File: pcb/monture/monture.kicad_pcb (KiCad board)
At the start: 2 copper layers, 150 x 110 mm, 72 parts, among them U1 Teensy 4.1

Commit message: PCB monture : deux cartes, StepStick et drivers externes
Carte StepStick (pcb/monture) :
- Selecteur retire (SW_SEL, RN_SEL, 74HC126/74HCT125, pastilles EXT) :
  les supports sont pilotes directement par le Teensy ; rappels RN_EN
  (10k vers 3,3V) pour garder les drivers coupes au demarrage.
- Ponts SPI TMC5160 conserves (decales de 0,1 mm : courtyards KiCad 10).
- Re-routage Freerouting, buck manuel conserve : DRC 0 erreur, 0 non
  connecte. Assemblage FreeCAD : modele PCB reimporte, 0 collision.

Carte drivers externes (pcb/monture_ext, nouvelle) :
- Par axe : bornier J_VM (VM, GND) et bornier J_SIG (EN, STEP, DIR, GND)
  en 5 V via 3 x 74HCT125 ; 220 uF par sortie VM ; plans GND et +36V.
- Meme format, fixations, connecteurs et brochage Teensy que la carte
  StepStick. DRC 0 erreur, 0 non connecte.
- Boitier 35 mm (boitier_monture_ext.scad), STL, rendus, assemblage
  FreeCAD controle.

build_kicad_pcbs.py genere les deux cartes (blocs communs) et reproduit
exactement les cartes routees. README et fiche technique mis a jour.

Co-Authored-By: Claude Opus 5.5 <noreply@anthropic.com>
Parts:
- removed C_EXT_DIR, C_EXT_EN, C_EXT_STEP, C_INT_DIR, C_INT_EN, C_INT_STEP: 100nF, C_Disc_D3.0mm_W1.6mm_P2.50mm
- removed EXT_ALT, EXT_AZ, EXT_DEROT, EXT_FOCUS: Ext. Driver, SolderWire-0.5sqmm_1x04_P4.6mm_D0.9mm_OD2.1mm
- removed RN_SEL: 10k x8 (commun broche 1), R_Array_SIP9
- removed SW_SEL: DIP x4, SW_DIP_SPSTx04_Slide_9.78x12.34mm_W7.62mm_P2.54mm
- removed U_EXT_DIR, U_EXT_EN, U_EXT_STEP: 74HCT125, DIP-14_W7.62mm
- removed U_INT_DIR, U_INT_EN, U_INT_STEP: 74HC126, DIP-14_W7.62mm
- added RN_EN: 10k x4 (commun broche 1), R_Array_SIP5, F.Cu at (108.0, 57.6)
- moved JP_DEROT_CLK 0.10 mm to (87.2, 48.7)
- moved JP_DEROT_CSN 0.10 mm to (87.2, 43.6)
- moved JP_DEROT_SCK 0.10 mm to (87.2, 41.1)
- moved JP_DEROT_SDI 0.10 mm to (87.2, 38.5)
- moved JP_DEROT_SDO 0.10 mm to (87.2, 46.2)
- moved JP_FOCUS_CLK 0.10 mm to (117.2, 48.7)
- moved JP_FOCUS_CSN 0.10 mm to (117.2, 43.6)
- moved JP_FOCUS_SCK 0.10 mm to (117.2, 41.1)
- moved JP_FOCUS_SDI 0.10 mm to (117.2, 38.5)
- moved JP_FOCUS_SDO 0.10 mm to (117.2, 46.2)
- moved JP_ALT_CLK 0.10 mm to (57.1, 48.7)
- moved JP_ALT_CSN 0.10 mm to (57.1, 43.6)
- moved JP_ALT_SCK 0.10 mm to (57.1, 41.1)
- moved JP_ALT_SDI 0.10 mm to (57.1, 38.5)
- moved JP_ALT_SDO 0.10 mm to (57.1, 46.2)
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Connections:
- DRV_ALT_L pad 1: ALT_EN_INT -> ALT_EN
- DRV_ALT_L pad 7: ALT_STEP_INT -> ALT_STEP
- DRV_ALT_L pad 8: ALT_DIR_INT -> ALT_DIR
- DRV_AZ_L pad 1: AZ_EN_INT -> AZ_EN
- DRV_AZ_L pad 7: AZ_STEP_INT -> AZ_STEP
- DRV_AZ_L pad 8: AZ_DIR_INT -> AZ_DIR
- DRV_DEROT_L pad 1: DEROT_EN_INT -> DEROT_EN
- DRV_DEROT_L pad 7: DEROT_STEP_INT -> DEROT_STEP
- DRV_DEROT_L pad 8: DEROT_DIR_INT -> DEROT_DIR
- DRV_FOCUS_L pad 1: FOCUS_EN_INT -> FOCUS_EN
- DRV_FOCUS_L pad 7: FOCUS_STEP_INT -> FOCUS_STEP
- DRV_FOCUS_L pad 8: FOCUS_DIR_INT -> FOCUS_DIR
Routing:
- net GND: track 733.1 -> 542.4 mm
- net AZ_EN_EXT: track 152.4 -> 0.00 mm, vias 1 -> 0
- net FOCUS_STEP_EXT: track 148.1 -> 0.00 mm, vias 2 -> 0
- net SEL_AZ: track 139.0 -> 0.00 mm
- net SEL_ALT: track 133.0 -> 0.00 mm, vias 2 -> 0
- net AZ_EN_INT: track 126.7 -> 0.00 mm
- net ALT_EN_EXT: track 124.2 -> 0.00 mm, vias 2 -> 0
- net SEL_FOCUS: track 123.1 -> 0.00 mm
- net SEL_DEROT: track 121.6 -> 0.00 mm
- net AZ_DIR_EXT: track 118.4 -> 0.00 mm, vias 2 -> 0
- net FOCUS_DIR_EXT: track 118.2 -> 0.00 mm, vias 1 -> 0
- net ALT_EN_INT: track 114.4 -> 0.00 mm, vias 3 -> 0
- net DEROT_STEP_EXT: track 104.1 -> 0.00 mm, vias 2 -> 0
- net FOCUS_EN_EXT: track 101.7 -> 0.00 mm, vias 1 -> 0
- net ALT_DIR_EXT: track 96.5 -> 0.00 mm, vias 3 -> 0
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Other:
- outline, holes or cut-outs redrawn
- board text added: "RAPPELS EN"
- board text removed: "ALT"
- board text removed: "AZ"
- board text removed: "DER"
- board text removed: "DIR"
- board text removed: "DRIVER EXT. 5V"
- board text removed: "FOC"
- board text removed: "GND"
- board text removed: "ON = EXTERNE 5V / OFF = STEPSTICK"
- board text removed: "SELECTEUR DRIVERS"
- board text removed: "STEP"
- board text removed: "TAMPONS DRIVERS EXTERNES 5V (74HCT125)"
- board text removed: "TAMPONS STEPSTICK 3,3V (74HC126)"

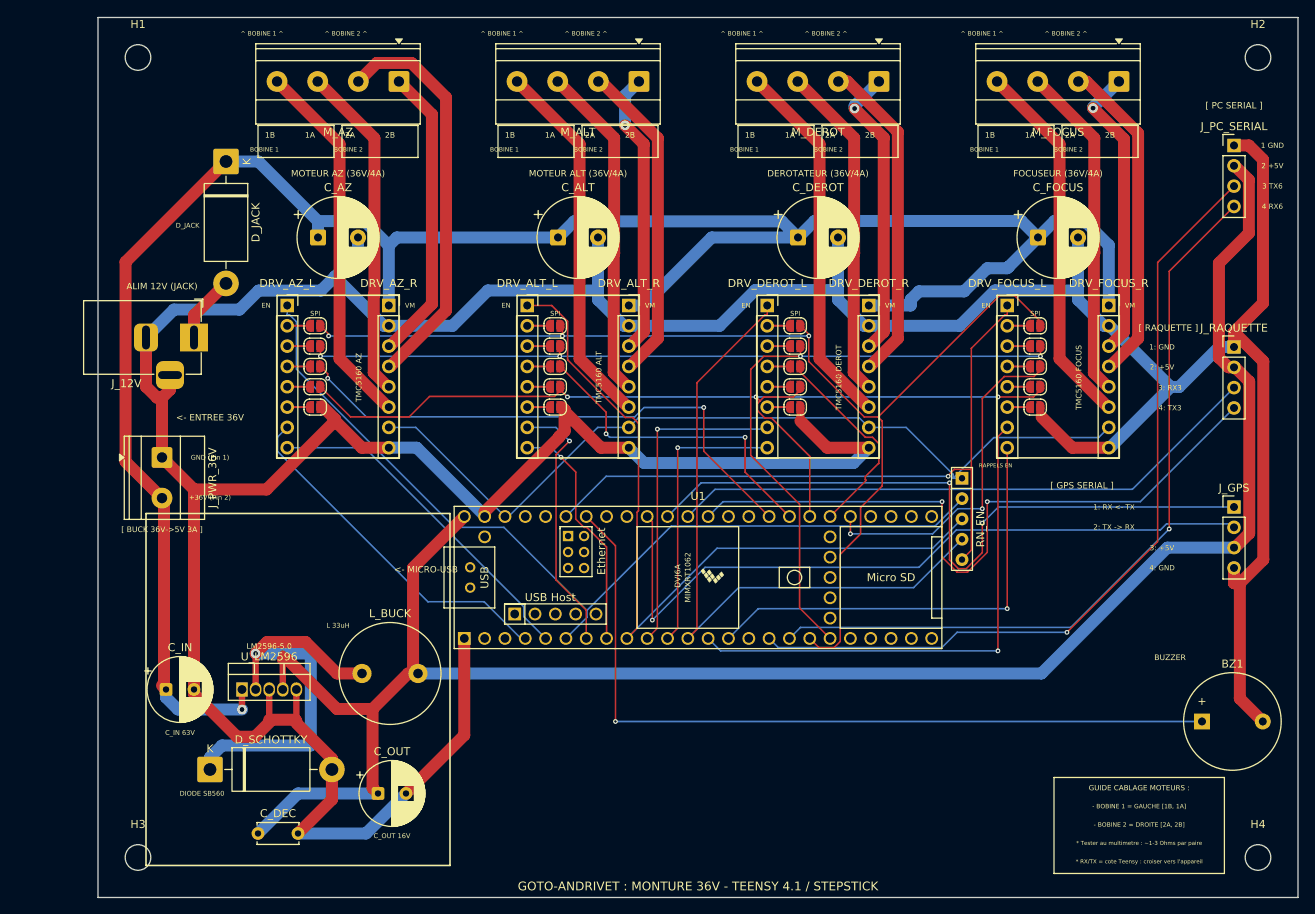
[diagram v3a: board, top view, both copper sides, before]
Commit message: Cartes : sérigraphie lisible, LM2596HV, 74ACT125, fichiers de fabrication
Sérigraphie des trois cartes refaite : tous les textes à 1 mm de haut et
0,15 mm de trait (règle DRC des .kicad_pro relevée à ces valeurs), plus
aucun texte sur un autre, sur une pastille ou hors de la carte.
- références des borniers dans leur bande libre, repères 1B/1A/2A/2B
  centrés sous les vis ;
- broches des connecteurs PC, raquette, GPS, LCD et Grove numérotées en
  face de chaque broche, côté Teensy (RX4/TX4, RX3/TX3, TX6/RX6) ;
- guides de câblage réécrits pour tenir en 1 mm ;
- cadre du buck retiré (il passait sur le trou H3 et le bornier 36V),
  références des trous de fixation masquées, marquages de la puce du
  Teensy passés sur la couche de fabrication ;
- raquette : titre centré (il sortait de la carte), repères sous chaque
  fil du câble vers la monture.
Cuivre, zones et pastilles inchangés (vérifiés identiques). DRC : 0
erreur, 0 non connecté ; seul reste l'avertissement du jack 12 V, qui
dépasse volontairement du bord.

Buck : LM2596HVT-5.0 (60 V en entrée) au lieu du LM2596-5.0 limité à
40 V sur un bus 36 V. Même boîtier, même brochage, même fréquence.

Carte drivers externes : 74ACT125 au lieu du 74HCT125. Entrées TTL
identiques, mais 24 mA par sortie au lieu de 6, pour les optocoupleurs
des drivers qui tirent 7 à 16 mA.

build_kicad_pcbs.py porte la nouvelle sérigraphie : il reproduit les
cartes routées. Nouveau fabrication.py : Gerber et perçages, liste des
composants regroupée par pièce à acheter, vues 3D, dans pcb/fabrication/.

Co-Authored-By: Claude Opus 5.5 <noreply@anthropic.com>
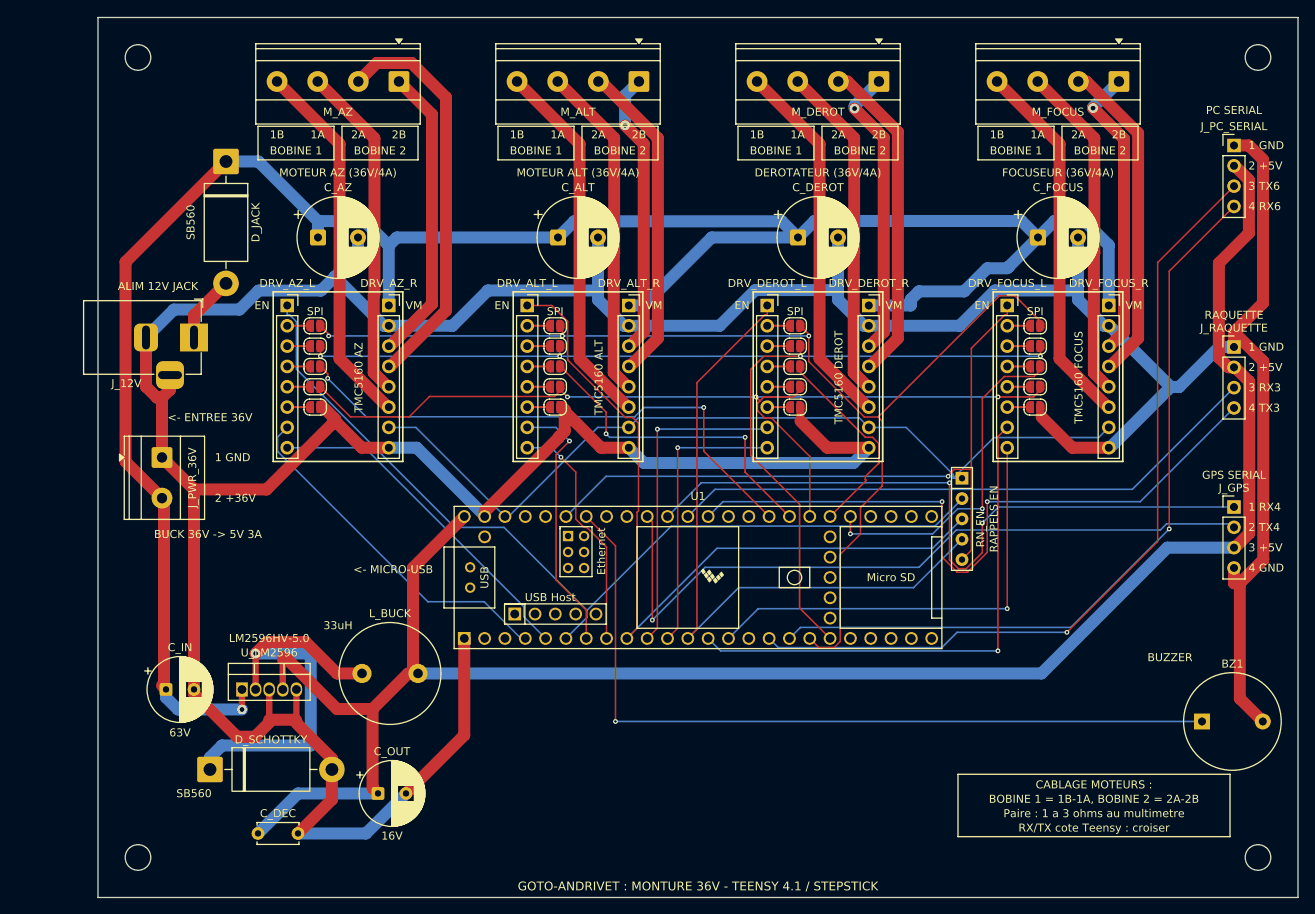
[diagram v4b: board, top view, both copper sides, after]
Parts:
- U_LM2596: value LM2596-5.0 -> LM2596HVT-5.0
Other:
- board text added: "1 RX4"
- board text added: "16V"
- board text added: "2 +36V"
- board text added: "2 TX4"
- board text added: "3 +5V"
- board text added: "3 RX3"
- board text added: "33uH"
- board text added: "4 GND"
- board text added: "4 TX3"
- board text added: "63V"
- board text added: "ALIM 12V JACK"
- board text added: "BOBINE 1 = 1B-1A, BOBINE 2 = 2A-2B"
- board text added: "BUCK 36V -> 5V 3A"
- board text added: "CABLAGE MOTEURS :"
- board text added: "GPS SERIAL"
- board text added: "LM2596HV-5.0"
- board text added: "PC SERIAL"
- board text added: "Paire : 1 a 3 ohms au multimetre"
- board text added: "RAQUETTE"
- board text added: "RX/TX cote Teensy : croiser"
- board text added: "SB560"
- board text removed: "* RX/TX = cote Teensy : croiser vers l'appareil"
- board text removed: "* Tester au multimetre : ~1-3 Ohms par paire"
- board text removed: "+36V (Pin 2)"
- board text removed: "- BOBINE 1 = GAUCHE [1B, 1A]"
- board text removed: "- BOBINE 2 = DROITE [2A, 2B]"
- board text removed: "1: GND"
- board text removed: "1: RX <- TX"
- board text removed: "2: +5V"
- board text removed: "2: TX -> RX"
- board text removed: "3: +5V"
- board text removed: "3: RX3"
- board text removed: "4: GND"
- board text removed: "4: TX3"
- board text removed: "ALIM 12V (JACK)"
- board text removed: "C_IN 63V"
- board text removed: "C_OUT 16V"
- board text removed: "DIODE SB560"
- board text removed: "D_JACK"
- board text removed: "GND (Pin 1)"
- board text removed: "GUIDE CABLAGE MOTEURS :"
- board text removed: "L 33uH"
- board text removed: "LM2596-5.0"
- board text removed: "[ BUCK 36V->5V 3A ]"
- board text removed: "[ GPS SERIAL ]"
- board text removed: "[ PC SERIAL ]"
- board text removed: "[ RAQUETTE ]"
- board text removed: "^ BOBINE 1 ^"
- board text removed: "^ BOBINE 2 ^"

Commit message: Cartes : protection de l'alimentation, buzzer sur transistor, I2C de la raquette en 3,3 V
Corrige les points trouvés à la vérification électrique (MCP KiCad).

Cartes monture (StepStick et drivers externes) :
- Entrée : D_JACK remplacée par D_IN, double diode Schottky MBR20100CT à
  cathode commune, une anode pour le bornier 36V et une pour le jack.
  Des fils inversés ou un jack à centre négatif ne passent plus ; puis
  F_IN, fusible TR5 temporisé 4 A sur support, commun aux deux entrées.
  Nouveaux réseaux PWR_IN et VIN_OR, en classe Puissance (1,5 mm).
- Buzzer : il était branché en direct sur la broche 20, alors qu'un
  buzzer passif tire 80 à 200 mA. Il est maintenant commandé par un
  PN2222A (1 kOhm sur la base, 10 kOhm de rappel au démarrage), alimenté
  en 5V à travers 68 Ohm, avec une diode 1N4148 à ses bornes.
- Sérigraphie « PC SERIAL 3V3 » : l'adaptateur USB-série doit être en
  3,3 V.

Carte raquette : adaptateur de niveau I2C à deux BSS138 (et quatre
10 kOhm). L'afficheur et la prise Grove restent en 5V ; le Teensy, qui
ne supporte pas le 5V, ne voit plus que du 3,3V sur SDA et SCL.

Routage refait par Freerouting (pistes du buck et amorces verrouillées
conservées, plans de cuivre de la carte externe remis). Deux broches OE
des 74ACT125, reliées au GND par piste, sont sorties du plan GND faute
de place pour leurs branches thermiques. DRC des trois cartes : 0
erreur, 0 non connecté ; le générateur reproduit exactement les cartes
routées. Assemblages FreeCAD mis à jour : aucune collision avec les
boîtiers ni avec les boutons.

Fichiers de fabrication, liste des composants, vues 3D, modèles .glb
et aperçus régénérés.

Co-Authored-By: Claude Opus 5.5 <noreply@anthropic.com>
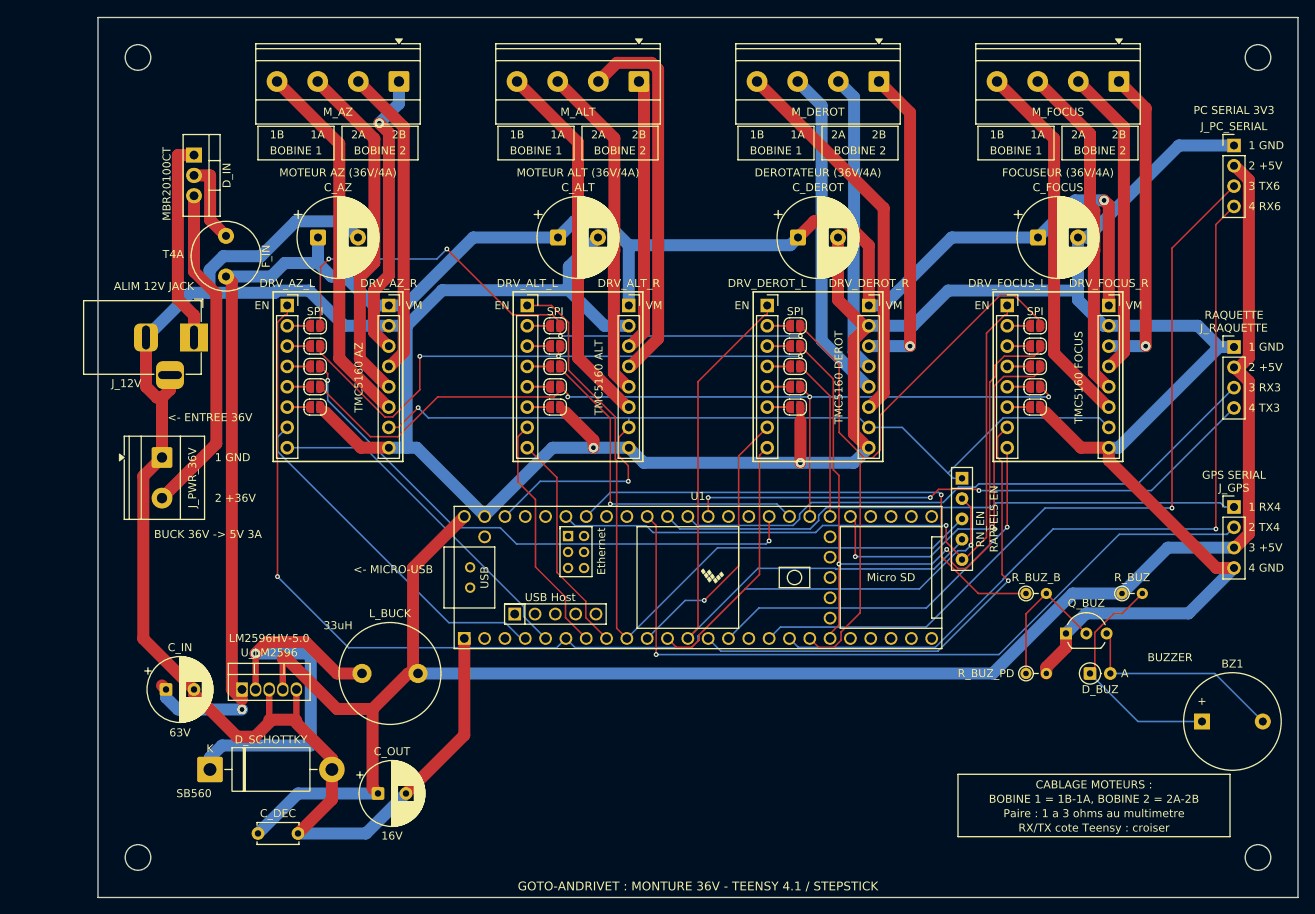
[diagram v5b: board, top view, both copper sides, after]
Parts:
- removed D_JACK: SB560 (60V 5A), D_DO-201AD_P15.24mm_Horizontal
- added D_BUZ: 1N4148, D_DO-35_SOD27_P2.54mm_Vertical_AnodeUp, F.Cu at (124.0, 82.0)
- added D_IN: MBR20100CT, TO-220-3_Vertical, F.Cu at (12.0, 17.2)
- added F_IN: T4A (TR5), Fuse_Littelfuse_372_D8.50mm, F.Cu at (16.0, 27.3)
- added Q_BUZ: PN2222A, TO-92_Inline_Wide, F.Cu at (121.0, 77.0)
- added R_BUZ: 68, R_Axial_DIN0204_L3.6mm_D1.6mm_P2.54mm_Vertical, F.Cu at (128.0, 72.0)
- added R_BUZ_B: 1k, R_Axial_DIN0204_L3.6mm_D1.6mm_P2.54mm_Vertical, F.Cu at (116.0, 72.0)
- added R_BUZ_PD: 10k, R_Axial_DIN0204_L3.6mm_D1.6mm_P2.54mm_Vertical, F.Cu at (116.0, 82.0)
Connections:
- BZ1 pad 1: BUZZER -> BUZ_A
- BZ1 pad 2: GND -> BUZ_C
- J_PWR_36V pad 2: +36V -> PWR_IN
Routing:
- net +36V: track 274.7 -> 225.8 mm, vias 1 -> 2
- net PWR_IN: track 0.00 -> 41.8 mm
- net BUZZER: track 100.5 -> 66.0 mm
- net BUZ_A: track 0.00 -> 29.8 mm
- net BUZ_C: track 0.00 -> 26.7 mm
- net SPI_SCK: track 139.7 -> 163.4 mm, vias 4 -> 5
- net AZ_EN: track 114.7 -> 137.8 mm, vias 0 -> 2
- net +3V3: track 106.9 -> 126.0 mm, vias 0 -> 2
- net BUZ_B: track 0.00 -> 18.1 mm
- net JACK_IN: track 8.42 -> 25.6 mm
- net SPI_MOSI: track 143.0 -> 158.4 mm, vias 3 -> 4
- net GPS_RX: track 88.0 -> 73.4 mm, vias 2 -> 0
- net RAQUETTE_TX: track 86.4 -> 72.9 mm, vias 2 -> 3
- net AZ_2A: track 50.4 -> 38.8 mm
- net VIN_OR: track 0.00 -> 10.4 mm
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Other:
- board text added: "MBR20100CT"
- board text added: "PC SERIAL 3V3"
- board text added: "T4A"
- board text removed: "PC SERIAL"
